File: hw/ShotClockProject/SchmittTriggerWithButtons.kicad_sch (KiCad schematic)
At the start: 10 parts, among them SW3 SW_SPST, SW4 SW_SPST, SW5 SW_SPST, U3 M74HC14YRM13TR

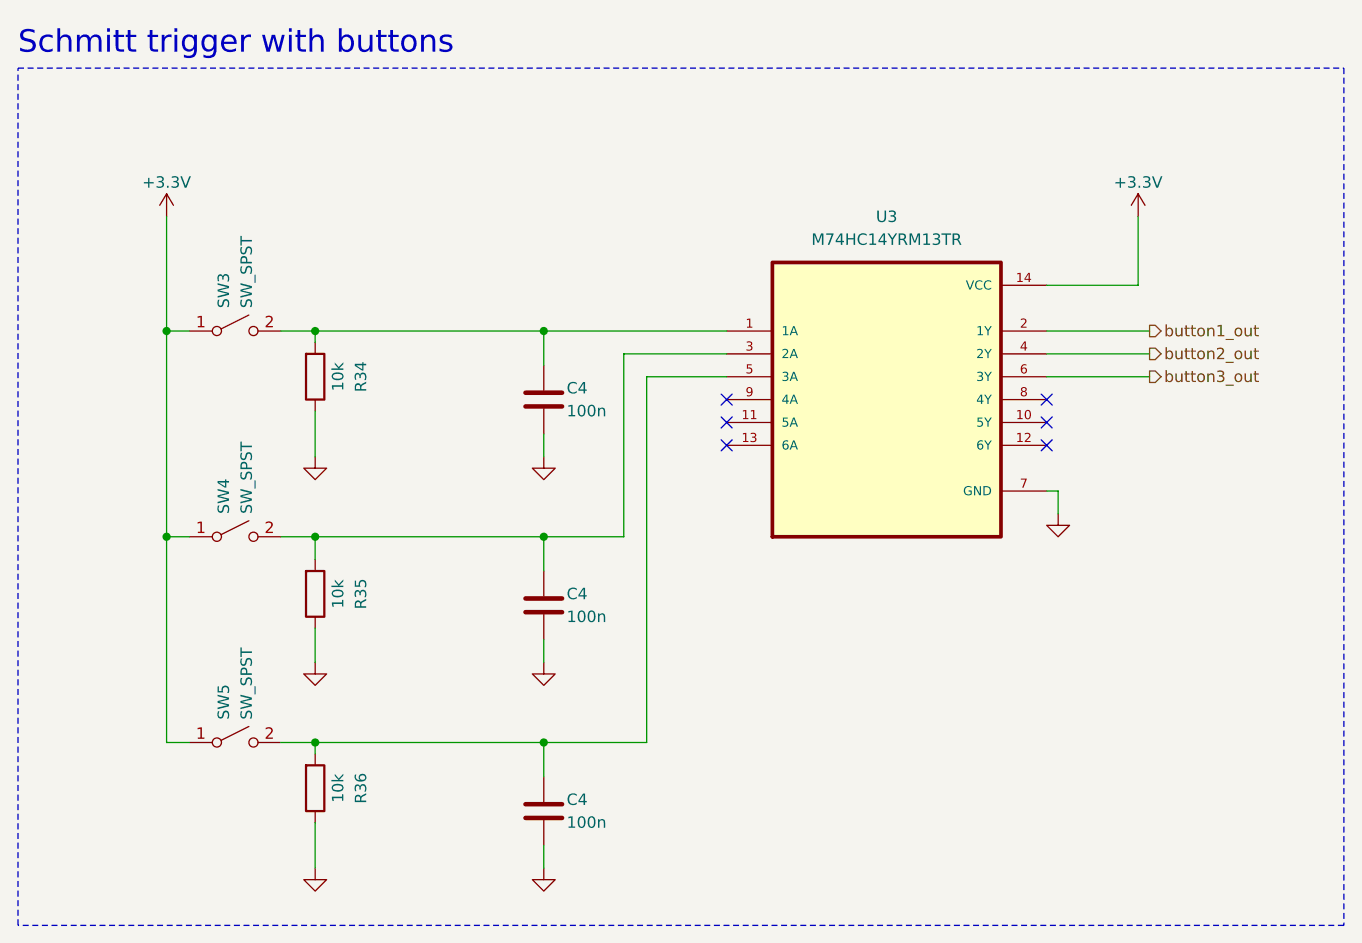
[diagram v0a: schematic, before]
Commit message: Redid layout with new board dimensions
Changed tactile switches to larger push switches (also momentary)
Changed USART1 to UART4 & added UART5 to STDC14 connector
Placed all components nearer to each other, and within the PCB outer edge
Added rounded corners
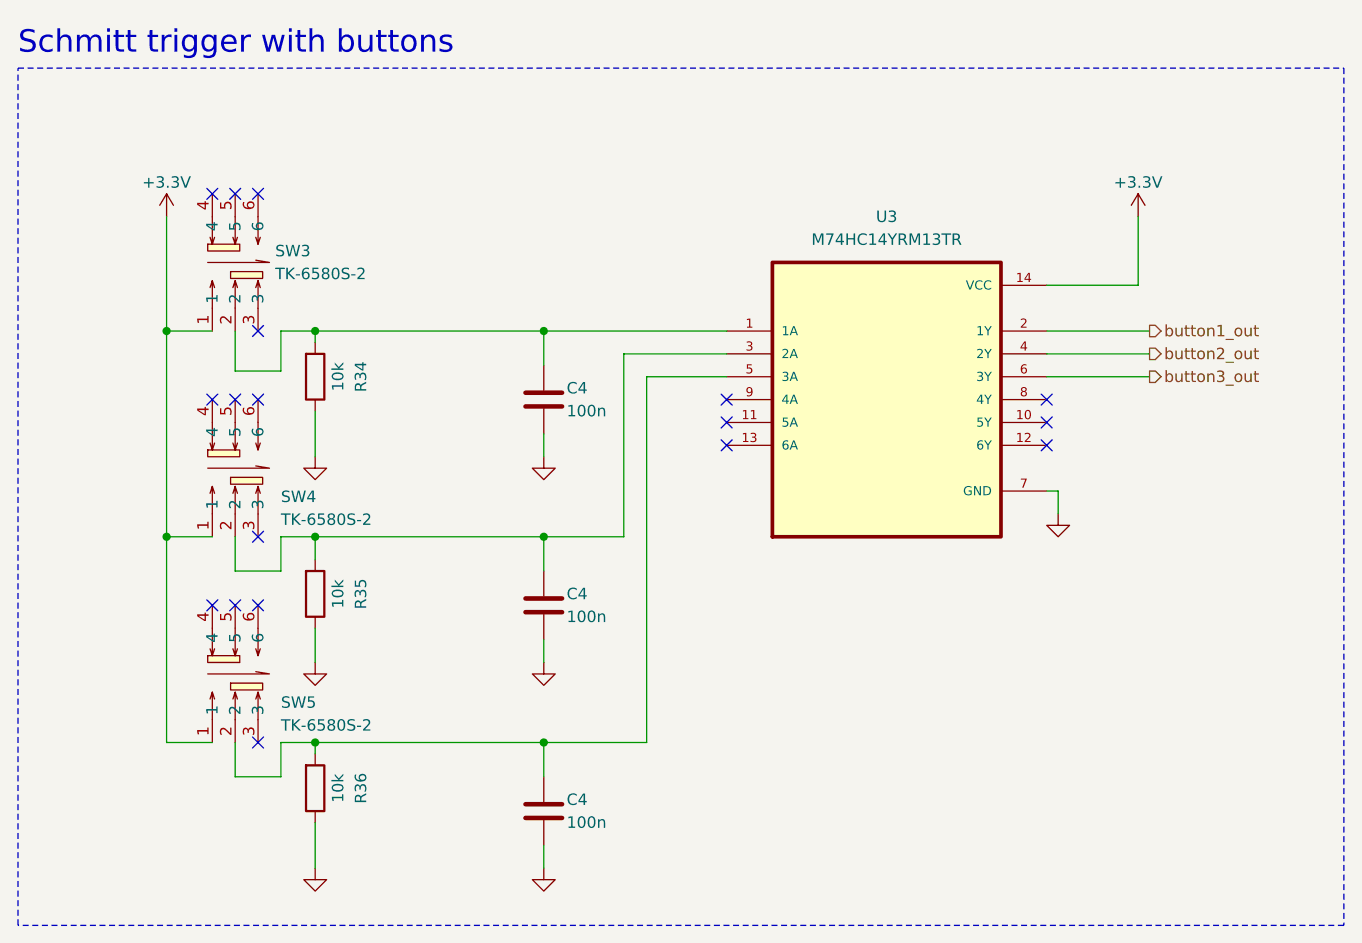
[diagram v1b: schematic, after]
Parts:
- removed SW3, SW4, SW5: SW_SPST, Button_Switch_SMD:SW_SPST_B3U-1000P, symbol Switch:SW_SPST
- added SW3, SW4, SW5: TK-6580S-2, TK-6580S-2:SW-SMD_TK-6580S-2, symbol TK-6580S-2:TK-6580S-2
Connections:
- net +3.3V: now also SW3.1, SW4.1, SW5.1
- net at C4.1, R35.2, U3.3 (2A): now also SW4.2
- net at C4.1, R34.2, U3.1 (1A): now also SW3.2
- net at C4.1, R36.2, U3.5 (3A): now also SW5.2
- no-connect marks 6 -> 18

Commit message: Added LCSC Part number
Renamed output folders
Created first output files for REV1
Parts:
- C4: LCSC Part (none) -> C1525; LCSC Part # (none) -> C1525
- R34, R35, R36: LCSC Part (none) -> C25744; LCSC Part # (none) -> C25744
- SW3, SW4, SW5: LCSC Part # (none) -> C528775
- U3: LCSC Part (none) -> C157450; LCSC Part # (none) -> C157450
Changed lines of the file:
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@@
       (effects (font (size 1.27 1.27)) (justify bottom) hide)
+    )
+    (property "LCSC Part #" "C157450" (at 176.53 85.09 0)
+      (effects (font (size 1.27 1.27)) hide)
+    )
+    (property "LCSC Part" "C157450" (at 176.53 85.09 0)
+      (effects (font (size 1.27 1.27)) hide)
     )
     (pin "1")
@@
       (effects (font (size 1.27 1.27)) hide)
     )
+    (property "LCSC Part #" "C1525" (at 138.43 85.09 0)
+      (effects (font (size 1.27 1.27)) hide)
+    )
+    (property "LCSC Part" "C1525" (at 138.43 85.09 0)
+      (effects (font (size 1.27 1.27)) hide)
+    )
     (pin "1")
     (pin "2")
@@
       (effects (font (size 1.27 1.27)) hide)
     )
-    (property "LCSC Part" "C528775" (at 104.14 87.63 0)
+    (property "LCSC Part #" "C528775" (at 104.14 69.85 0)
+      (effects (font (size 1.27 1.27)) hide)
+    )
+    (property "LCSC Part" "C528775" (at 104.14 69.85 0)
       (effects (font (size 1.27 1.27)) hide)
     )
@@
       (effects (font (size 1.27 1.27)) hide)
     )
+    (property "LCSC Part #" "C25744" (at 113.03 106.68 0)
+      (effects (font (size 1.27 1.27)) hide)
+    )
+    (property "LCSC Part" "C25744" (at 113.03 106.68 0)
+      (effects (font (size 1.27 1.27)) hide)
+    )
     (pin "1")
     (pin "2")
@@
       (effects (font (size 1.27 1.27)) hide)
     )
+    (property "LCSC Part #" "C1525" (at 138.43 130.81 0)
+      (effects (font (size 1.27 1.27)) hide)
+    )
+    (property "LCSC Part" "C1525" (at 138.43 130.81 0)
+      (effects (font (size 1.27 1.27)) hide)
+    )
     (pin "1")
     (pin "2")
@@
       (effects (font (size 1.27 1.27)) hide)
     )
+    (property "LCSC Part #" "C25744" (at 113.03 82.55 0)
+      (effects (font (size 1.27 1.27)) hide)
+    )
+    (property "LCSC Part" "C25744" (at 113.03 82.55 0)
+      (effects (font (size 1.27 1.27)) hide)
+    )
     (pin "1")
     (pin "2")
@@
       (effects (font (size 1.27 1.27)) hide)
     )
-    (property "LCSC Part" "C528775" (at 104.14 110.49 0)
+    (property "LCSC Part #" "C528775" (at 104.14 92.71 0)
+      (effects (font (size 1.27 1.27)) hide)
+    )
+    (property "LCSC Part" "C528775" (at 104.14 92.71 0)
       (effects (font (size 1.27 1.27)) hide)
     )
@@
       (effects (font (size 1.27 1.27)) hide)
     )
+    (property "LCSC Part #" "C1525" (at 138.43 107.95 0)
+      (effects (font (size 1.27 1.27)) hide)
+    )
+    (property "LCSC Part" "C1525" (at 138.43 107.95 0)
+      (effects (font (size 1.27 1.27)) hide)
+    )
     (pin "1")
     (pin "2")
@@
       (effects (font (size 1.27 1.27)) hide)
     )
+    (property "LCSC Part #" "C25744" (at 113.03 128.27 0)
+      (effects (font (size 1.27 1.27)) hide)
+    )
+    (property "LCSC Part" "C25744" (at 113.03 128.27 0)
+      (effects (font (size 1.27 1.27)) hide)
+    )
     (pin "1")
     (pin "2")
@@
       (effects (font (size 1.27 1.27)) hide)
     )
-    (property "LCSC Part" "C528775" (at 104.14 133.35 0)
-      (effects (font (size 1.27 1.27)) hide)
-    )
+    (property "LCSC Part #" "C528775" (at 104.14 115.57 0)
+      (effects (font (size 1.27 1.27)) hide)
+    )
+    (property "LCSC Part" "C528775" (at 104.14 115.57 0)
+      (effects (font (size 1.27 1.27)) hide)
+    )

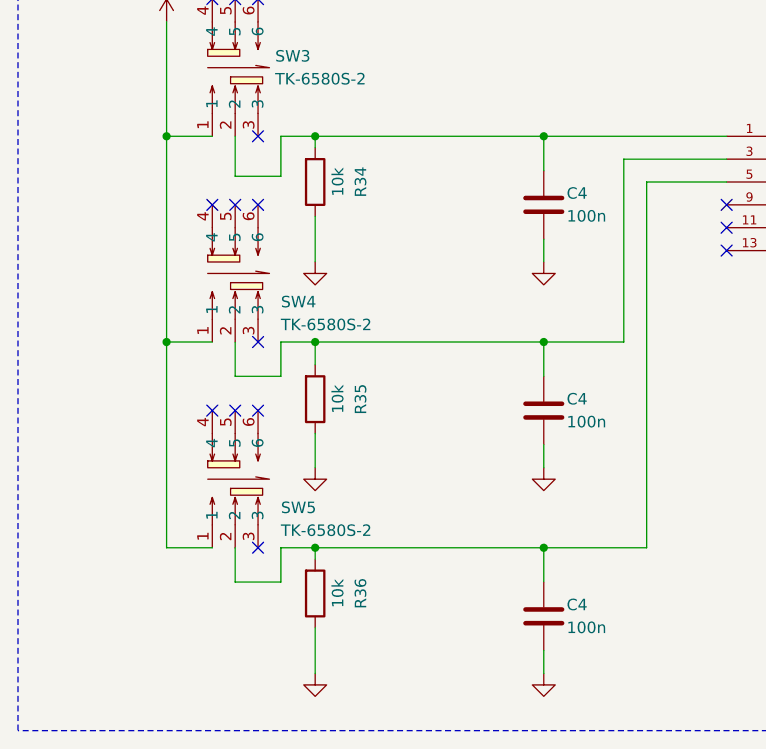
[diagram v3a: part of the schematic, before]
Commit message: Added I2C support
Calculated pull-up resistor values
Added 6 pin female headers to mainboard
Added nRESET line for the I2C chips
Removed PCB routing and part placement
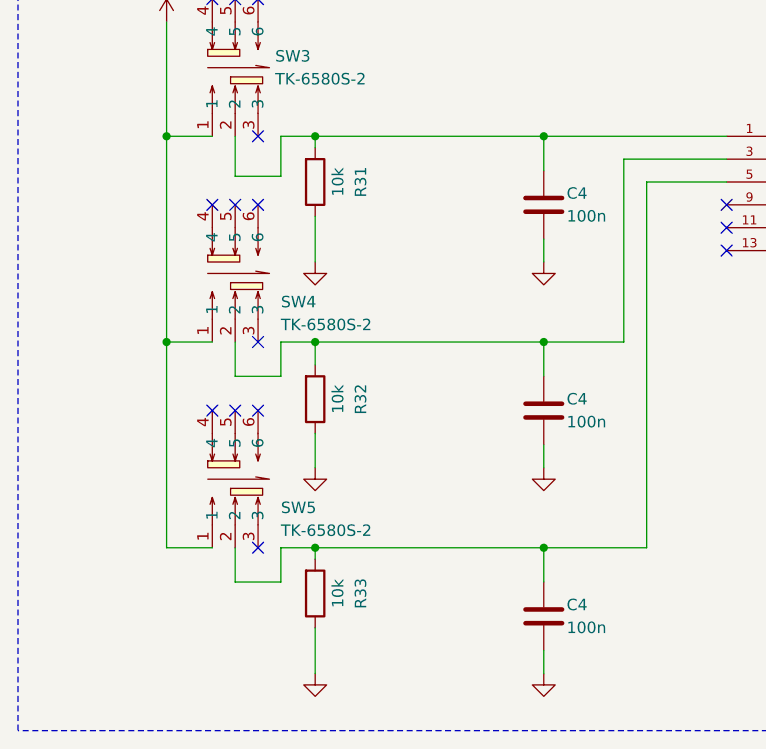
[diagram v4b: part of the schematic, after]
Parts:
- renumbered R34 to R31, R35 to R32, R36 to R33
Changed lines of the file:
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@@
         )
         (path "/5fd859aa-754d-49c2-9762-3f7ebe3bb64c/1ce26b90-d7f5-4886-998a-a021d351eec6"
-          (reference "C28") (unit 1)
+          (reference "C27") (unit 1)
         )
       )
@@
   (symbol (lib_id "Device:R") (at 113.03 106.68 0) (mirror x) (unit 1)
     (in_bom yes) (on_board yes) (dnp no)
-    (property "Reference" "R35" (at 118.11 106.68 90)
+    (property "Reference" "R32" (at 118.11 106.68 90)
       (effects (font (size 1.27 1.27)))
     )
@@
       (project "ShotClockProject"
         (path "/5fd859aa-754d-49c2-9762-3f7ebe3bb64c/1ce26b90-d7f5-4886-998a-a021d351eec6"
-          (reference "R35") (unit 1)
+          (reference "R32") (unit 1)
         )
       )
@@
         )
         (path "/5fd859aa-754d-49c2-9762-3f7ebe3bb64c/1ce26b90-d7f5-4886-998a-a021d351eec6"
-          (reference "#PWR069") (unit 1)
+          (reference "#PWR063") (unit 1)
         )
       )
@@
         )
         (path "/5fd859aa-754d-49c2-9762-3f7ebe3bb64c/1ce26b90-d7f5-4886-998a-a021d351eec6"
-          (reference "#PWR073") (unit 1)
+          (reference "#PWR067") (unit 1)
         )
       )
@@
         )
         (path "/5fd859aa-754d-49c2-9762-3f7ebe3bb64c/1ce26b90-d7f5-4886-998a-a021d351eec6"
-          (reference "#PWR074") (unit 1)
+          (reference "#PWR068") (unit 1)
         )
       )
@@
         )
         (path "/5fd859aa-754d-49c2-9762-3f7ebe3bb64c/1ce26b90-d7f5-4886-998a-a021d351eec6"
-          (reference "C30") (unit 1)
+          (reference "C29") (unit 1)
         )
       )
@@
         )
         (path "/5fd859aa-754d-49c2-9762-3f7ebe3bb64c/1ce26b90-d7f5-4886-998a-a021d351eec6"
-          (reference "#PWR076") (unit 1)
+          (reference "#PWR070") (unit 1)
         )
       )
@@
         )
         (path "/5fd859aa-754d-49c2-9762-3f7ebe3bb64c/1ce26b90-d7f5-4886-998a-a021d351eec6"
-          (reference "#PWR070") (unit 1)
+          (reference "#PWR064") (unit 1)
         )
       )
@@
   (symbol (lib_id "Device:R") (at 113.03 82.55 0) (mirror x) (unit 1)
     (in_bom yes) (on_board yes) (dnp no)
-    (property "Reference" "R34" (at 118.11 82.55 90)
+    (property "Reference" "R31" (at 118.11 82.55 90)
       (effects (font (size 1.27 1.27)))
     )
@@
       (project "ShotClockProject"
         (path "/5fd859aa-754d-49c2-9762-3f7ebe3bb64c/1ce26b90-d7f5-4886-998a-a021d351eec6"
-          (reference "R34") (unit 1)
+          (reference "R31") (unit 1)
         )
       )
@@
         )
         (path "/5fd859aa-754d-49c2-9762-3f7ebe3bb64c/1ce26b90-d7f5-4886-998a-a021d351eec6"
-          (reference "#PWR071") (unit 1)
+          (reference "#PWR065") (unit 1)
         )
       )
@@
         )
         (path "/5fd859aa-754d-49c2-9762-3f7ebe3bb64c/1ce26b90-d7f5-4886-998a-a021d351eec6"
-          (reference "#PWR077") (unit 1)
+          (reference "#PWR071") (unit 1)
         )
       )
@@
         )
         (path "/5fd859aa-754d-49c2-9762-3f7ebe3bb64c/1ce26b90-d7f5-4886-998a-a021d351eec6"
-          (reference "C29") (unit 1)
+          (reference "C28") (unit 1)
         )
       )
@@
         )
         (path "/5fd859aa-754d-49c2-9762-3f7ebe3bb64c/1ce26b90-d7f5-4886-998a-a021d351eec6"
-          (reference "#PWR072") (unit 1)
+          (reference "#PWR066") (unit 1)
         )
       )
@@
         )
         (path "/5fd859aa-754d-49c2-9762-3f7ebe3bb64c/1ce26b90-d7f5-4886-998a-a021d351eec6"
-          (reference "#PWR075") (unit 1)
+          (reference "#PWR069") (unit 1)
         )
       )
@@
   (symbol (lib_id "Device:R") (at 113.03 128.27 0) (mirror x) (unit 1)
     (in_bom yes) (on_board yes) (dnp no)
-    (property "Reference" "R36" (at 118.11 128.27 90)
+    (property "Reference" "R33" (at 118.11 128.27 90)
       (effects (font (size 1.27 1.27)))
     )
@@
       (project "ShotClockProject"
         (path "/5fd859aa-754d-49c2-9762-3f7ebe3bb64c/1ce26b90-d7f5-4886-998a-a021d351eec6"
-          (reference "R36") (unit 1)
-        )
-      )
+          (reference "R33") (unit 1)
+        )
+      )

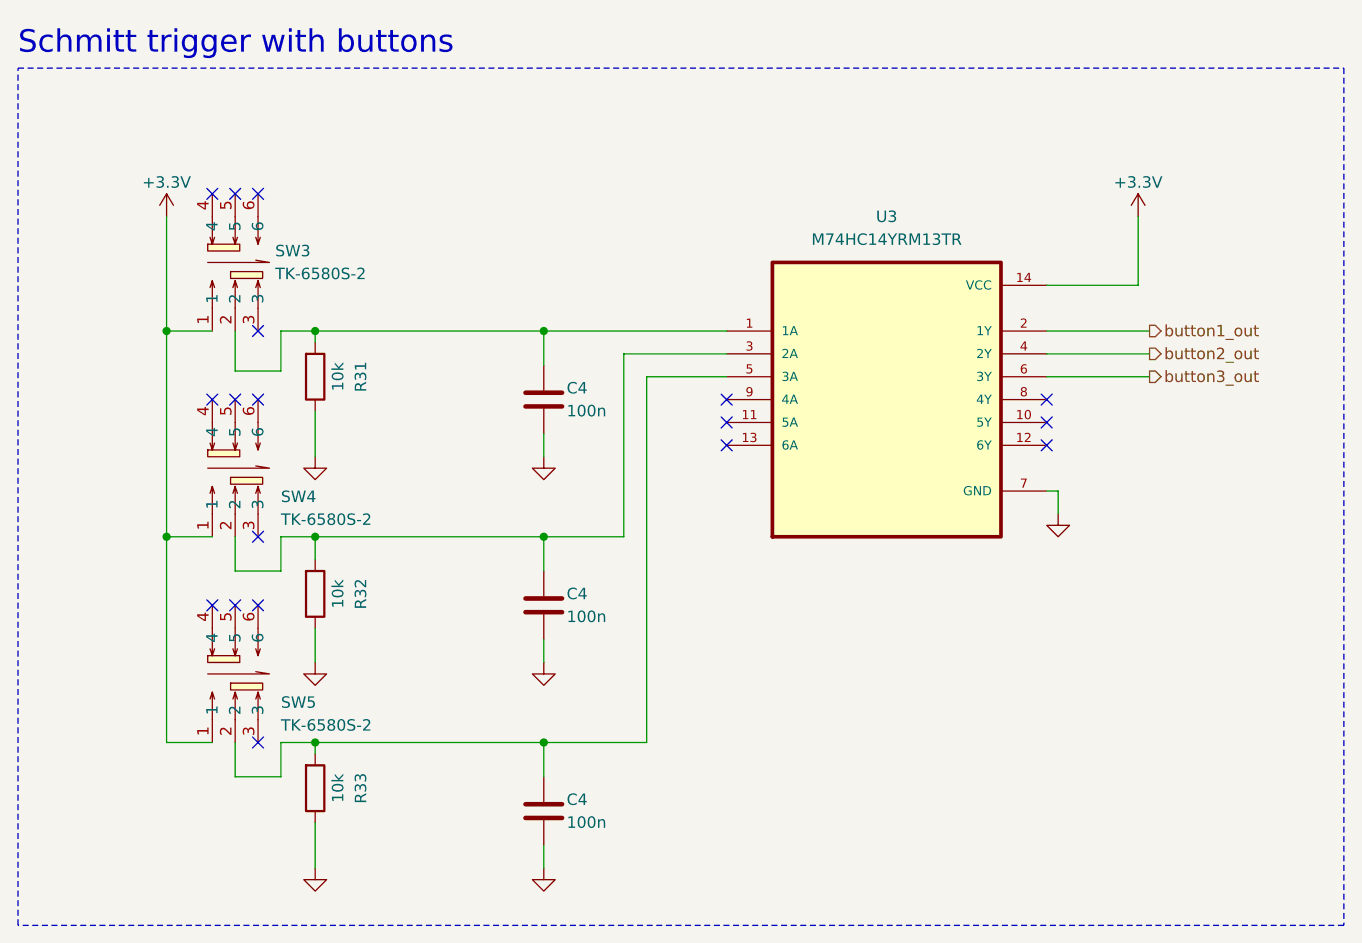
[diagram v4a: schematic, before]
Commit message: Finished mainboard routing
Reconfigered pins to make routing easier/cleaner
Placed copper fills as much as possible to create an even plating index
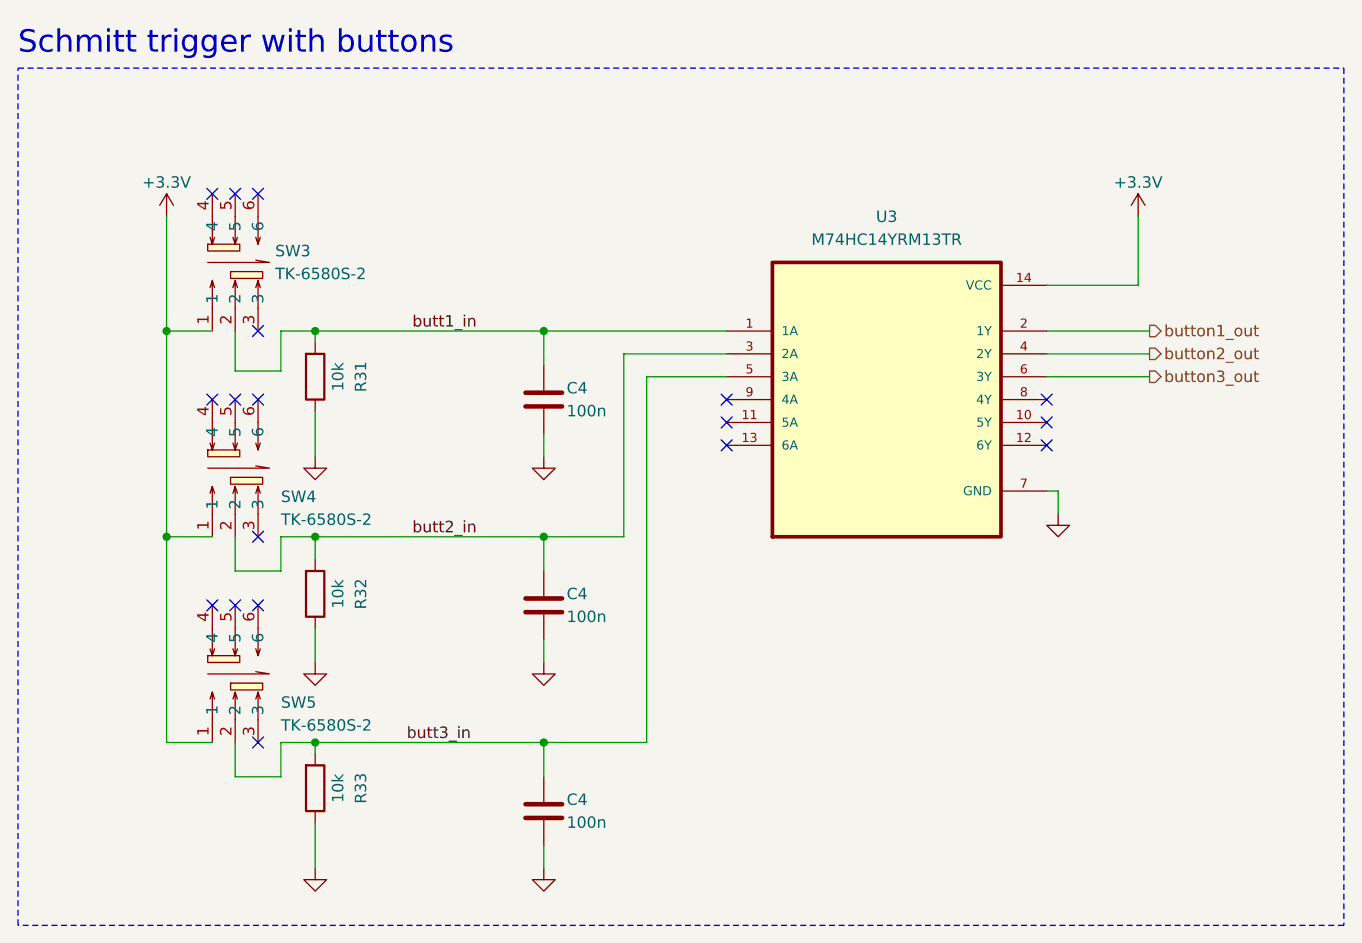
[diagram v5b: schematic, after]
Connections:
- net butt1_in: now reaches C4.1, R31.2, SW3.2, U3.1 (1A)
- net butt2_in: now reaches C4.1, R32.2, SW4.2, U3.3 (2A)
- net butt3_in: now reaches C4.1, R33.2, SW5.2, U3.5 (3A)
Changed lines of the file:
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@@
     (effects (font (size 2.5 2.5) (color 255 0 0 1)) (justify left bottom))
+  )
+  (label "butt3_in" (at 123.19 123.19 0) (fields_autoplaced)
+    (effects (font (size 1.27 1.27)) (justify left bottom))
+  )
+  (label "butt1_in" (at 123.825 77.47 0) (fields_autoplaced)
+    (effects (font (size 1.27 1.27)) (justify left bottom))
+  )
+  (label "butt2_in" (at 123.825 100.33 0) (fields_autoplaced)
+    (effects (font (size 1.27 1.27)) (justify left bottom))
   )
   (hierarchical_label "button3_out" (shape output) (at 205.74 82.55 0) (fields_autoplaced)
